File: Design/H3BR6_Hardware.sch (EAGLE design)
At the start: 64 parts, among them P2 HEXABIT_X2_P1_P5, Q10 MMBT3904LT1, Q11 MMBT3904LT1, Q12 MMBT3904LT1, Q13 MMBT3904LT1, Q14 MMBT3904LT1, Q7 MMBT3904LT1, Q8 MMBT3904LT1, Q9 MMBT3904LT1, U1 STM32F072CBT6STMICROELECTRONI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, X1 XTALL_CSTCE8M00G52

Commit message: Release REV0
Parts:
- U1: value STM32F072CBT6STMICROELECTRONICS_STM32F072CBT6_0_0 -> (none); device HEXABITZ_ICs:STM32F072CBT6STMICROELECTRONICS_STM32F072CBT6_0_0 -> HEXABITZ_ICs:STM32F091CBU6
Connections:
- net GND: now also U1.EP, U1.VSS_0, U1.VSS_1, U1.VSS_2; no longer U1.1_VSS, U1.2_VSS, U1.3_VSS
- net N$7: now also U1.PF11-OSC_BOOT0; no longer U1.BOOT0
- net N$8: now also U1.NRST; no longer U1.!RST!
- net VDD: now also U1.VDD_0, U1.VDD_1; no longer U1.1_VDD, U1.2_VDD
- net VSSA: now also U1.VSS_A; no longer U1.VSSA
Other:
- note added: "0"
- moved on the sheet: B, C, C8, D, D1, R, R1, R3, X1

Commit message: FIX Rev0
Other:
- note added: "Salah Souda"
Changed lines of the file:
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@@
 <setting verticaltext="up"/>
 </settings>
-<grid distance="0.05" unitdist="inch" unit="mil" style="lines" multiple="1" display="no" altdistance="0.01" altunitdist="inch" altunit="inch"/>
+<grid distance="25" unitdist="mil" unit="mil" style="lines" multiple="1" display="no" altdistance="0.01" altunitdist="inch" altunit="inch"/>
 <layers>
 <layer number="1" name="Top" color="4" fill="1" visible="no" active="no"/>
@@
 <text x="243.1962" y="5.7422" size="1.9304" layer="100" font="vector">www.hexabitz.com</text>
 <text x="31.03" y="197.69" size="1.778" layer="150">VDD=3.3 Volts</text>
+<text x="182.7442" y="4.5992" size="1.9304" layer="101" font="vector">Salah Souda</text>
 </plain>
 <instances>
@@
 <wire x1="231.69" y1="17.858" x2="231.69" y2="22.43" width="0.1524" layer="205"/>
 <text x="243.1962" y="5.7422" size="1.9304" layer="100" font="vector">www.hexabitz.com</text>
+<text x="184.0142" y="4.5992" size="1.9304" layer="101" font="vector">Salah Souda</text>
 </plain>
 <instances>

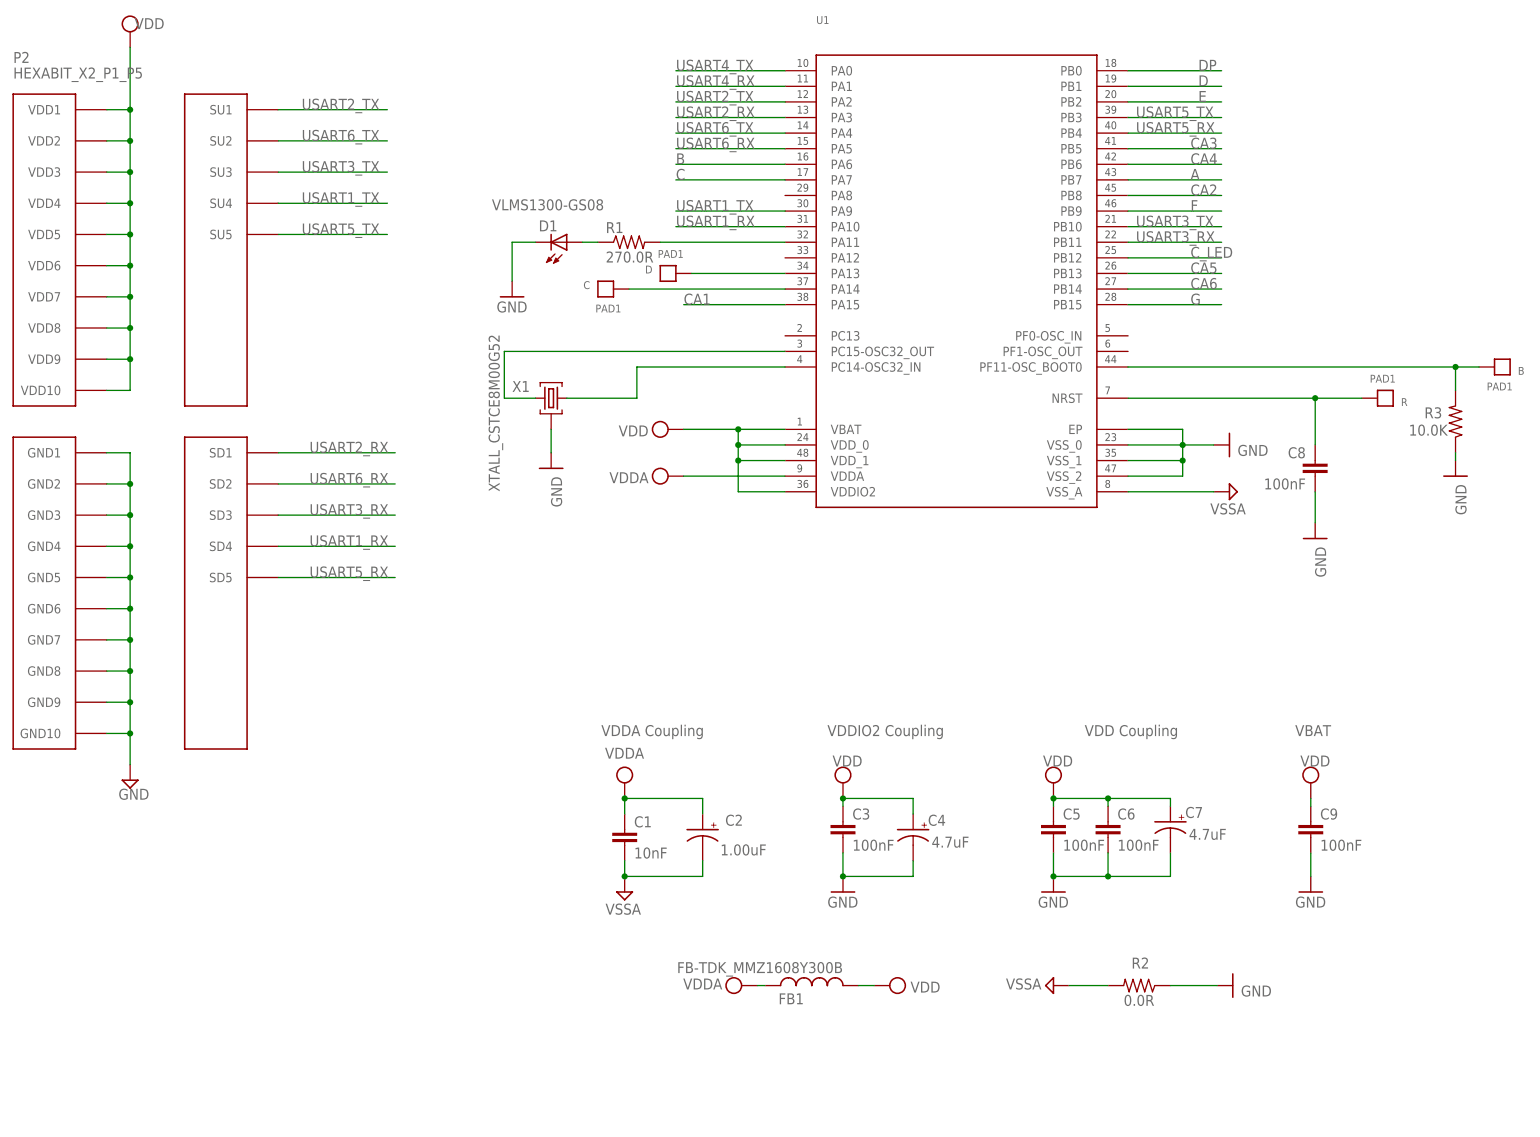
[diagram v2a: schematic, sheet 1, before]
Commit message: -Changing the MC with STM32G0
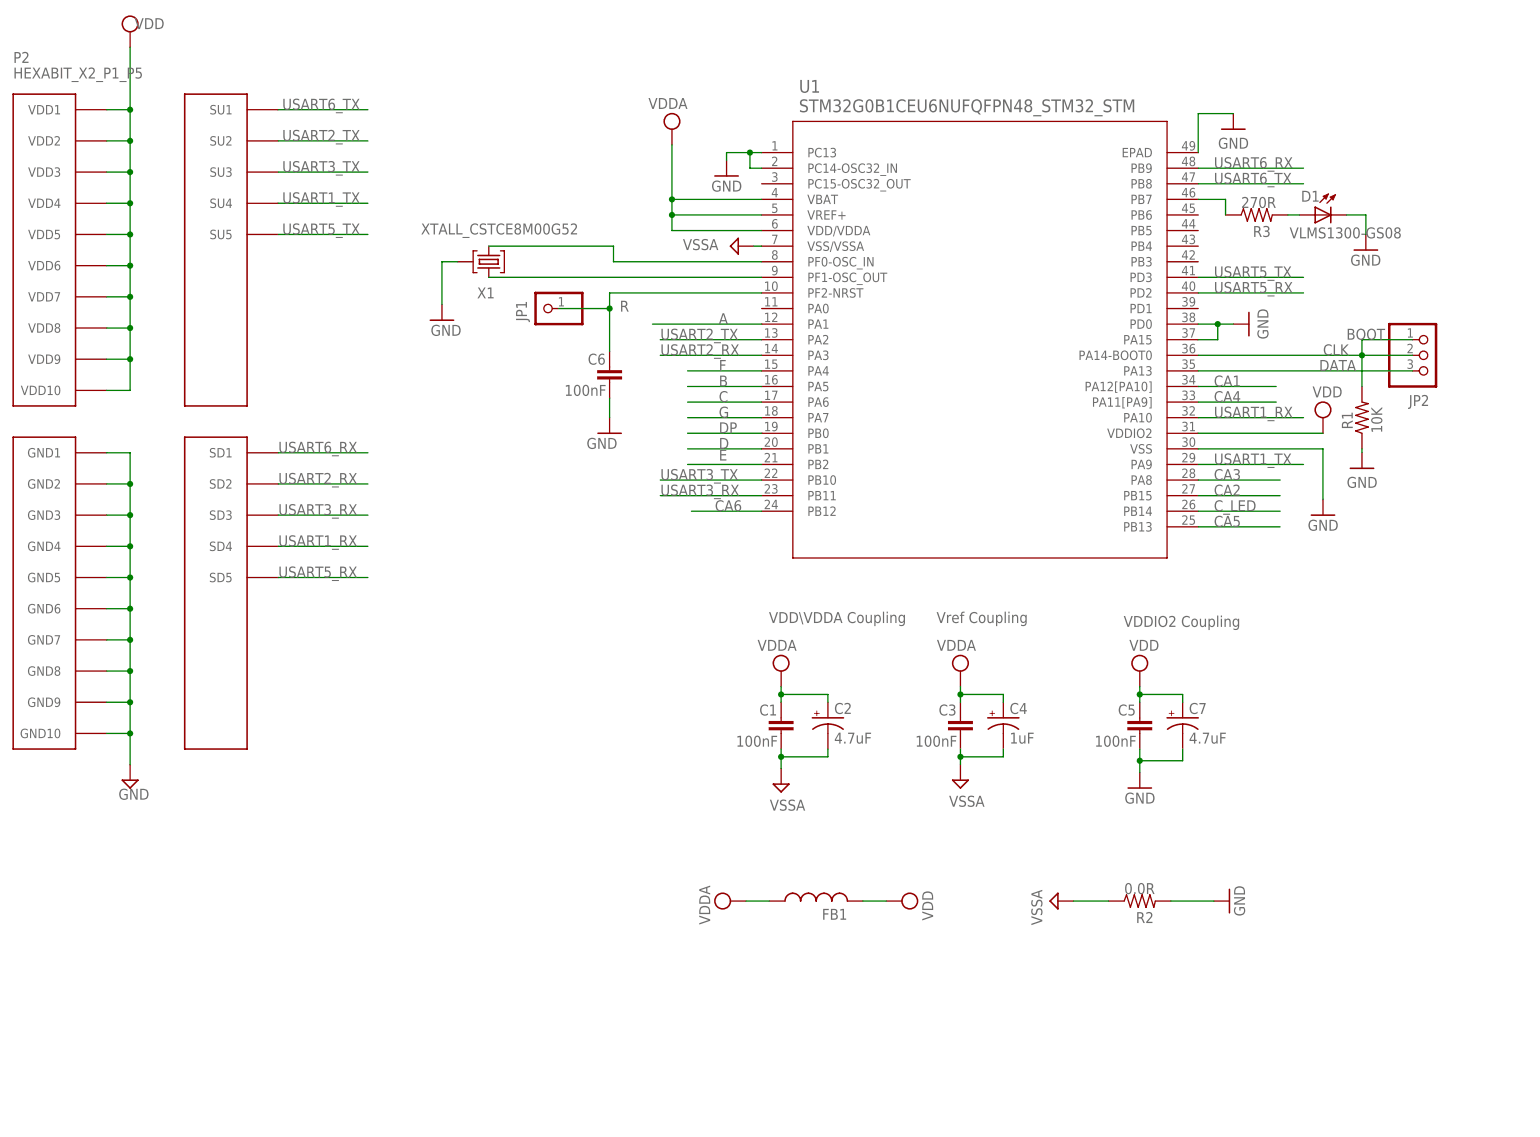
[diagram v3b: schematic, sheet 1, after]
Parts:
- removed B, C, D, R: PAD1, Hexabitz:PAD1
- removed C8, C9: 100nF, Hexabitz:C-0603
- added JP1: R, HEXABITZ_USER_INTERFACE_PARTS:PINHD-1X1
- added JP2: (no value), pinhead:PINHD-1X3
- C1: value 10nF -> 100nF; device Hexabitz:C-0603 -> HEXABITZ_RCLS:C-0603; CAPACITANCE 10nF -> (none); MFN KEMET -> (none); MPN C0603C103K5RACTU -> (none); OCTOPART_URL https://octopart.com/c0603c103k5ractu-kemet-133094?r=sp&s=R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 -> (none); TOLERANCE 10% -> (none); VOLTAGE_RATING 50V -> (none)
- C2: value 1.00uF -> 4.7uF; device Hexabitz:C-0805-POL -> HEXABITZ_RCLS:C-0805-POL; CAPACITANCE 1.00uF -> (none); MFN Yageo -> (none); MPN CC0805KKX7R7BB105 -> (none); OCTOPART_URL https://octopart.com/cc0805kkx7r7bb105-yageo-8376555?r=sp&s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 -> (none); TOLERANCE 10% -> (none); VOLTAGE_RATING 16V -> (none)
- C3, C6: device Hexabitz:C-0603 -> HEXABITZ_RCLS:C-0603; CAPACITANCE 100nF -> (none); MFN KEMET -> (none); MPN C0603C104K8RACTU -> (none); OCTOPART_URL https://octopart.com/c0603c104k8ractu-kemet-145075?r=sp&s=9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 -> (none); TOLERANCE 10% -> (none); VOLTAGE_RATING 10V -> (none)
- C4: value 4.7uF -> 1uF; device Hexabitz:C-0805-POL -> HEXABITZ_RCLS:C-0805-POL; CAPACITANCE 4.7uF -> (none); MFN Murata -> (none); MPN GRM21BC81E475KA12L -> (none); OCTOPART_URL https://octopart.com/grm21bc81e475ka12l-murata-10331911?r=s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 -> (none); TOLERANCE 10% -> (none); VOLTAGE_RATING 25V -> (none)
- C5: device Hexabitz:C-0603 -> HEXABITZ_RCLS:C-0603; CAPACITANCE 100nF -> (none); MFN KEMET -> (none); MPN C0603C104K8RACTU -> (none); OCTOPART_URL https://octopart.com/c0603c104k8ractu-kemet-145075?r=sp&s=9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 -> (none); TOLERANCE 10% -> (none); VOLTAGE_RATING 10 -> (none)
- C7: device Hexabitz:C-0805-POL -> HEXABITZ_RCLS:C-0805-POL; CAPACITANCE 4.7uF -> (none); MFN Murata -> (none); MPN GRM21BC81E475KA12L -> (none); OCTOPART_URL https://octopart.com/grm21bc81e475ka12l-murata-10331911?r=s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 -> (none); TOLERANCE 10% -> (none); VOLTAGE_RATING 25V -> (none)
- FB1: value FB-TDK_MMZ1608Y300B -> (none); device Hexabitz:FB-TDK_MMZ1608Y300B -> HEXABITZ_RCLS:FB-0603; MFN TDK -> (none); MPN MMZ1608Y300B -> (none); OCTOPART_URL https://octopart.com/mmz1608y300b-tdk-368280?r=sp&s=cd9_2ZE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 -> (none)
- LED1, LED2, LED3, LED4: device HEXABITZ_RCLS:LED3MM -> led:LED3MM
- R1: value 270.0R -> 10K; device Hexabitz:R-0603 -> HEXABITZ_RCLS:R-0603; MFN Yageo -> (none); MPN RC0603FR-07270RL -> (none); OCTOPART_URL https://octopart.com/search?q=RC0603FR-07270RL&start=0 -> (none); RESISTANCE 270.0 Ohm -> (none); TOLERANCE 5% -> (none)
- R10, R11, R20, R21, R22, R23, R24, R25, R26, R4, R5, R6, R7, R8, R9: value 10K -> 10k; device Hexabitz:R-0603 -> HEXABITZ_RCLS:R-0603; MFN Yageo -> (none); MPN RC0603JR-071KL -> (none); RESISTANCE 1K Ohm -> (none); TOLERANCE 5% -> (none)
- R12, R13, R14, R15, R16, R17, R18, R19: device Hexabitz:R-0603 -> HEXABITZ_RCLS:R-0603; MFN Yageo -> (none); MPN RC0603JR-07220RL -> (none); RESISTANCE 220 Ohm -> (none); TOLERANCE 5% -> (none)
- R2: device Hexabitz:R-0603 -> HEXABITZ_RCLS:R-0603; MFN Yageo -> (none); MPN RC0603JR-070RL -> (none); OCTOPART_URL https://octopart.com/rc0603jr-070rl-yageo-1241539?r=sp&s=X2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 -> (none); RESISTANCE 0.0 Ohm -> (none)
- R3: value 10.0K -> 270R; device Hexabitz:R-0603 -> HEXABITZ_RCLS:R-0603; MFN Yageo -> (none); MPN RC0603JR-0710KL -> (none); OCTOPART_URL https://octopart.com/search?q=RC0603JR-0710KL&start=0 -> (none); RESISTANCE 10.0K Ohm -> (none); TOLERANCE 5% -> (none)
- U1: value (none) -> STM32G0B1CEU6NUFQFPN48_STM32_STM; device HEXABITZ_ICs:STM32F091CBU6 -> HEXABITZ_ICs:STM32G0B1CEU6NUFQFPN48_STM32_STM
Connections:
- removed net N$3: D.P$1, U1.PA13
- removed net N$4: C.P$1, U1.PA14
- removed net N$7: B.P$1, R3.2, U1.PF11-OSC_BOOT0
- removed net USART4_RX: U1.PA1
- removed net USART4_TX: U1.PA0
- new net CLK: JP2.1, JP2.2, R1.2, U1.PA14-BOOT0
- new net DATA: JP2.3, U1.PA13
- net A: now also R26.1, U1.PA1; no longer R4.2, U1.PB7
- net B: now also R25.1, U1.PA5; no longer R5.2, U1.PA6
- net C: now also R24.1, U1.PA6; no longer R6.2, U1.PA7
- net CA1: now also R4.1, U1.PA12[PA10]; no longer R20.2, U1.PA15
- net CA2: now also R5.1, U1.PB15; no longer R21.2, U1.PB8
- net CA3: now also R6.1, U1.PA8; no longer R22.2, U1.PB5
- net CA4: now also R7.1, U1.PA11[PA9]; no longer R23.2, U1.PB6
- net CA5: now also R8.1; no longer R24.2
- net CA6: now also R9.1, U1.PB12; no longer R25.2, U1.PB14
- net C_LED: now also R10.1, U1.PB14; no longer R26.2, U1.PB12
- net D: now also R23.1; no longer R7.2
- net DP: now also R11.1; no longer R11.2
- net E: now also R22.1; no longer R8.2
- net F: now also R21.1, U1.PA4; no longer R9.2, U1.PB9
- net G: now also R20.1, U1.PA7; no longer R10.2, U1.PB15
- net GND: now also R1.1, R2.2, U1.EPAD, U1.PA15, U1.PC13, U1.PC14-OSC32_IN, U1.PD0, U1.VSS; no longer C3.2, C4.-, C8.2, C9.2, R2.1, R3.1, U1.EP, U1.VSS_0, U1.VSS_1, U1.VSS_2
- net N$1: now also R3.2; no longer R1.1
- net N$10: now also R25.2; no longer R5.1
- net N$11: now also R24.2; no longer R6.1
- net N$12: now also R23.2; no longer R7.1
- net N$13: now also R22.2; no longer R8.1
- net N$14: now also R21.2; no longer R9.1
- net N$15: now also R20.2; no longer R10.1
- net N$16: now also R11.2; no longer R11.1
- net N$17: now also R12.1; no longer R12.2
- net N$18: now also R13.1; no longer R13.2
- net N$19: now also R14.1; no longer R14.2
- net N$2: now also R3.1, U1.PB7; no longer R1.2, U1.PA11
- net N$20: now also R15.1; no longer R15.2
- net N$21: now also R16.1; no longer R16.2
- net N$22: now also R17.1; no longer R17.2
- net N$23: now also R18.1; no longer R18.2
- net N$24: now also R19.1; no longer R19.2
- net N$25: now also R4.2; no longer R20.1
- net N$26: now also R5.2; no longer R21.1
- net N$27: now also R6.2; no longer R22.1
- net N$28: now also R7.2; no longer R23.1
- net N$29: now also R8.2; no longer R24.1
- net N$30: now also R9.2; no longer R25.1
- net N$31: now also R19.2; no longer R19.1
- net N$32: now also R18.2; no longer R18.1
- net N$33: now also R17.2; no longer R17.1
- net N$34: now also R16.2; no longer R16.1
- net N$35: now also R15.2; no longer R15.1
- net N$36: now also R14.2; no longer R14.1
- net N$37: now also R13.2; no longer R13.1
- net N$38: now also R12.2; no longer R12.1
- net N$45: now also R10.2; no longer R26.1
- net N$5: now also U1.PF1-OSC_OUT; no longer U1.PC14-OSC32_IN
- net N$6: now also U1.PF0-OSC_IN; no longer U1.PC15-OSC32_OUT
- net N$8: now also C6.1, JP1.1, U1.PF2-NRST; no longer C8.1, R.P$1, U1.NRST
- net N$9: now also R26.2; no longer R4.1
- net USART2_RX: now also P2.SD2; no longer P2.SD1
- net USART2_TX: now also P2.SU2; no longer P2.SU1
- net USART5_RX: now also U1.PD2; no longer U1.PB4
- net USART5_TX: now also U1.PD3; no longer U1.PB3
- net USART6_RX: now also P2.SD1, U1.PB9; no longer P2.SD2, U1.PA5
- net USART6_TX: now also P2.SU1, U1.PB8; no longer P2.SU2, U1.PA4
- net VDD: no longer C3.1, C4.+, C6.1, C9.1, U1.VBAT, U1.VDD_0, U1.VDD_1
- net VDDA: now also C3.1, C4.+, U1.VBAT, U1.VDD/VDDA, U1.VREF+; no longer U1.VDDA
- net VSSA: now also C3.2, C4.-, R2.1, U1.VSS/VSSA; no longer R2.2, U1.VSS_A
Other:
- note added: "BOOT"
- note added: "H3BR61"
- note added: "H3BR61_Backend"
- note added: "H3BR61_Frontend"
- note added: "Ibrahim Zaeiter"
- note added: "VDD\VDDA Coupling"
- note added: "Vref Coupling"
- note removed: "H3BR6"
- note removed: "H3BR6_Backend"
- note removed: "H3BR6_Frontend"
- note removed: "Salah Souda"
- note removed: "VBAT"
- note removed: "VDD Coupling"
- note removed: "VDDA Coupling"
- moved on the sheet: C1, C2, C3, C4, C5, C6, C7, D1, FB1, LED3, LED4, R1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
